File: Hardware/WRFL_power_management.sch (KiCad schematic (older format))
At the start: 42 parts, among them P1 JST_XH_2, P17 1x2_2_54_MALE, P2 TEST_POINT, P3 TEST_POINT, P4 JST_XH_2, P5 TEST_POINT, P6 TEST_POINT, P7 TEST_POINT, Q1 SI1012CR, Q2 SI2333DDS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

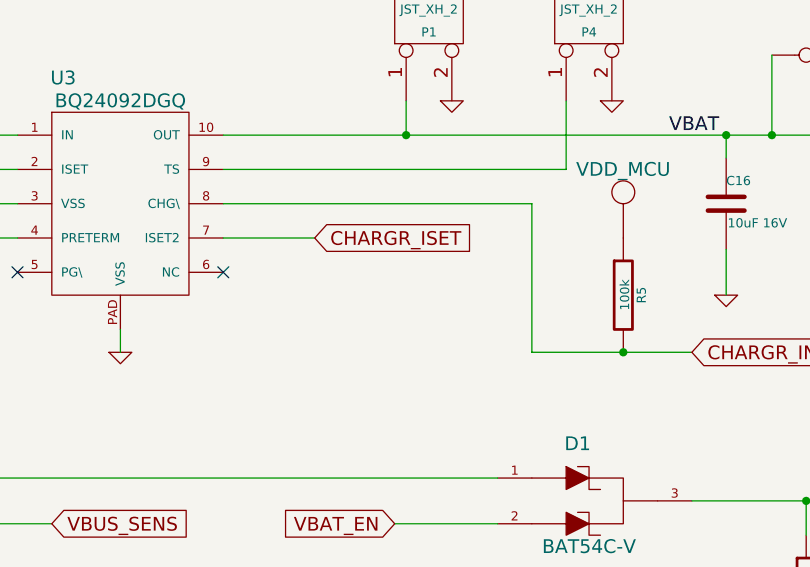
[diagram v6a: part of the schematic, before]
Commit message: Added BAT temp sens
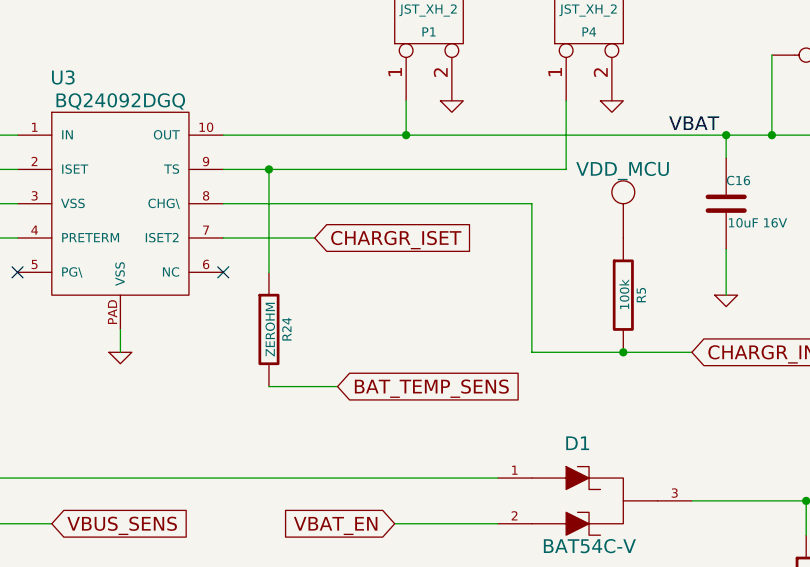
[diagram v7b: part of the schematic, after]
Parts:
- added R24: ZEROHM, 0805, symbol R
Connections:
- net at P4.1 (P1), U3.9 (TS): now also R24.1
- new net BAT_TEMP_SENS: R24.2

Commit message: on switch pull supply correction
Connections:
- net PM_ENABLE: no longer R14.2, R15.1
- net VDD_PERIPH: now also R14.2, R15.1
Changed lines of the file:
@@
-EESchema Schematic File Version 2  date Sunday, October 27, 2013 'AMt' 10:59:49 AM
+EESchema Schematic File Version 2  date 10/31/2013 11:19:55 PM
 LIBS:power
 LIBS:device
@@
 Sheet 2 6
 Title "WRFL power management"
-Date "27 oct 2013"
+Date "31 oct 2013"
 Rev "1.0"
 Comp "Nightmechanic"
@@
 $EndComp
 Wire Wire Line
-	3500 1300 6550 1300
+	3500 1300 4300 1300
+Wire Wire Line
+	4300 1300 5700 1300
+Wire Wire Line
+	5700 1300 5900 1300
+Wire Wire Line
+	5900 1300 6200 1300
+Wire Wire Line
+	6200 1300 6550 1300
 Wire Wire Line
 	6200 1400 6200 1300
@@
 Connection ~ 4300 1300
 Wire Wire Line
-	5000 1150 5000 1450
-Wire Wire Line
-	6750 1600 6750 2700
+	5000 1450 5000 1150
+Wire Wire Line
+	6750 1600 6750 2050
+Wire Wire Line
+	6750 2050 6750 2700
 Wire Wire Line
 	6200 1900 6200 2050
@@
 $EndComp
 Wire Wire Line
-	5550 2900 6450 2900
+	5550 2900 6050 2900
+Wire Wire Line
+	6050 2900 6450 2900
 Wire Wire Line
 	6050 2900 6050 3050
@@
 	6750 3100 6750 3650
 Wire Wire Line
-	7150 6050 8300 6050
+	7150 6050 7950 6050
+Wire Wire Line
+	7950 6050 8300 6050
 Text Label 5450 1300 0    60   ~ 0
 VBAT
@@
 	8150 6150 8150 6200
 Wire Wire Line
-	9000 6050 10550 6050
+	9000 6050 9550 6050
+Wire Wire Line
+	9550 6050 10350 6050
+Wire Wire Line
+	10350 6050 10550 6050
 $Comp
 L CONN_1 P2
@@
 $EndComp
 Wire Wire Line
-	1300 2300 1300 2900
+	1300 2300 1300 2800
+Wire Wire Line
+	1300 2800 1300 2900
 Connection ~ 6050 2900
 Wire Wire Line
-	1300 2800 4700 2800
+	1300 2800 2350 2800
+Wire Wire Line
+	2350 2800 4700 2800
 $Comp
 L GND #PWR3
@@
 	1300 3400 1300 3600
 Wire Wire Line
-	950  1300 2600 1300
+	950  1300 1300 1300
+Wire Wire Line
+	1300 1300 1550 1300
+Wire Wire Line
+	1550 1300 2600 1300
 Wire Wire Line
 	1300 1300 1300 1800
@@
 	3200 4550 3200 4750
 Wire Wire Line
-	2800 4400 5000 4400
+	2800 4400 3750 4400
+Wire Wire Line
+	3750 4400 4300 4400
+Wire Wire Line
+	4300 4400 5000 4400
 Wire Wire Line
 	3750 4400 3750 4750
@@
 $EndComp
 Wire Wire Line
-	4300 4250 4300 4650
+	4300 4250 4300 4400
+Wire Wire Line
+	4300 4400 4300 4650
 Text GLabel 4250 3000 0    60   Input ~ 0
 VBAT_EN
@@
 $EndComp
 Wire Wire Line
-	6950 1300 8050 1300
-Text GLabel 10550 2050 2    60   Input ~ 0
+	6950 1300 7300 1300
+Wire Wire Line
+	7300 1300 7700 1300
+Wire Wire Line
+	7700 1300 8050 1300
+Text GLabel 1200 6850 0    60   Input ~ 0
 PM_ENABLE
-Wire Wire Line
-	9650 2050 10550 2050
-Text Label 10000 2050 0    60   ~ 0
-PM_EN
 $Comp
 L LM2735Y U4
@@
 $EndComp
 Wire Wire Line
-	900  6000 2100 6000
+	900  6000 1200 6000
+Wire Wire Line
+	1200 6000 1700 6000
+Wire Wire Line
+	1700 6000 2100 6000
 Wire Wire Line
 	1200 6000 1200 6100
 Connection ~ 1700 6000
 Wire Wire Line
-	2700 6000 3450 6000
+	2700 6000 3100 6000
+Wire Wire Line
+	3100 6000 3450 6000
 Connection ~ 3100 6000
 Wire Wire Line
-	3850 6000 5250 6000
+	3850 6000 4100 6000
+Wire Wire Line
+	4100 6000 4400 6000
+Wire Wire Line
+	4400 6000 4600 6000
+Wire Wire Line
+	4600 6000 5100 6000
+Wire Wire Line
+	5100 6000 5250 6000
 Wire Wire Line
 	4600 6000 4600 6300
 Wire Wire Line
-	4100 6000 4100 6300
+	4100 6000 4100 6200
+Wire Wire Line
+	4100 6200 4100 6300
 Connection ~ 4100 6000
 Wire Wire Line
 	4100 6850 4100 6700
 Wire Wire Line
-	2900 6850 4100 6850
+	2900 6850 3800 6850
+Wire Wire Line
+	3800 6850 4100 6850
 Wire Wire Line
 	2900 6450 3100 6450
@@
 	1700 6450 1700 6000
 Wire Wire Line
-	3800 6800 3800 7000
+	3800 6800 3800 6850
+Wire Wire Line
+	3800 6850 3800 7000
 Connection ~ 3800 6850
 Wire Wire Line
@@
 $EndComp
 Wire Wire Line
-	900  5900 900  6100
+	900  5900 900  6000
+Wire Wire Line
+	900  6000 900  6100
 Connection ~ 1200 6000
 Wire Wire Line
-	1850 6850 1050 6850
+	1850 6850 1200 6850
 $Comp
 L V_BOOST #U5
@@
 Connection ~ 1300 2800
 Wire Wire Line
-	5000 1450 3500 1450
+	3500 1450 3700 1450
+Wire Wire Line
+	3700 1450 5000 1450
 $Comp
 L R R4
@@
 $EndComp
 Wire Wire Line
-	4850 2250 5550 2250
+	4850 2250 5250 2250
+Wire Wire Line
+	5250 2250 5550 2250
 Wire Wire Line
 	4850 2250 4850 1600
@@
 $EndComp
 Wire Wire Line
-	9850 2200 9850 2050
-Connection ~ 9850 2050
+	9850 1900 9850 2050
+Wire Wire Line
+	9850 2050 9850 2200
 Wire Wire Line
 	9850 2700 9850 2900
@@
 $EndComp
 Wire Wire Line
-	6200 2050 7400 2050
+	6200 2050 6750 2050
+Wire Wire Line
+	6750 2050 7400 2050
 Connection ~ 6750 2050
 Text Notes 7350 1700 0    60   ~ 0
@@
 	8950 3150 8950 3350
 Wire Wire Line
-	8950 3850 8950 4000
+	8950 3850 8950 3950
+Wire Wire Line
+	8950 3950 8950 4000
 Wire Wire Line
 	8950 4500 8950 4650
@@
 	900  6500 900  6550
 Wire Wire Line
-	900  6550 1200 6550
+	900  6550 1050 6550
+Wire Wire Line
+	1050 6550 1200 6550
 Wire Wire Line
 	1200 6550 1200 6500
@@
 Text GLabel 4000 2400 2    60   Input ~ 0
 BAT_TEMP_SENS
+$Comp
+L VDD_PERIPH #U?
+U 1 1 5272BAE9
+P 9850 1700
+F 0 "#U?" H 9850 1900 60  0001 C CNN
+F 1 "VDD_PERIPH" H 9850 1800 60  0000 C CNN
+F 2 "" H 9850 1700 60  0000 C CNN
+F 3 "" H 9850 1700 60  0000 C CNN
+	1    9850 1700
+	1    0    0    -1
+$EndComp
+Wire Wire Line
+	9650 2050 9850 2050
+Connection ~ 9850 2050
 $EndSCHEMATC
